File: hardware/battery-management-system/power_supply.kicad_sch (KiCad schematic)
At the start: 42 parts, among them J10 18V, J11 3V3, J9 5V, U1 ICL7660, U2 L6982C33DR, U3 L6982C33DR, U4 ICL7660

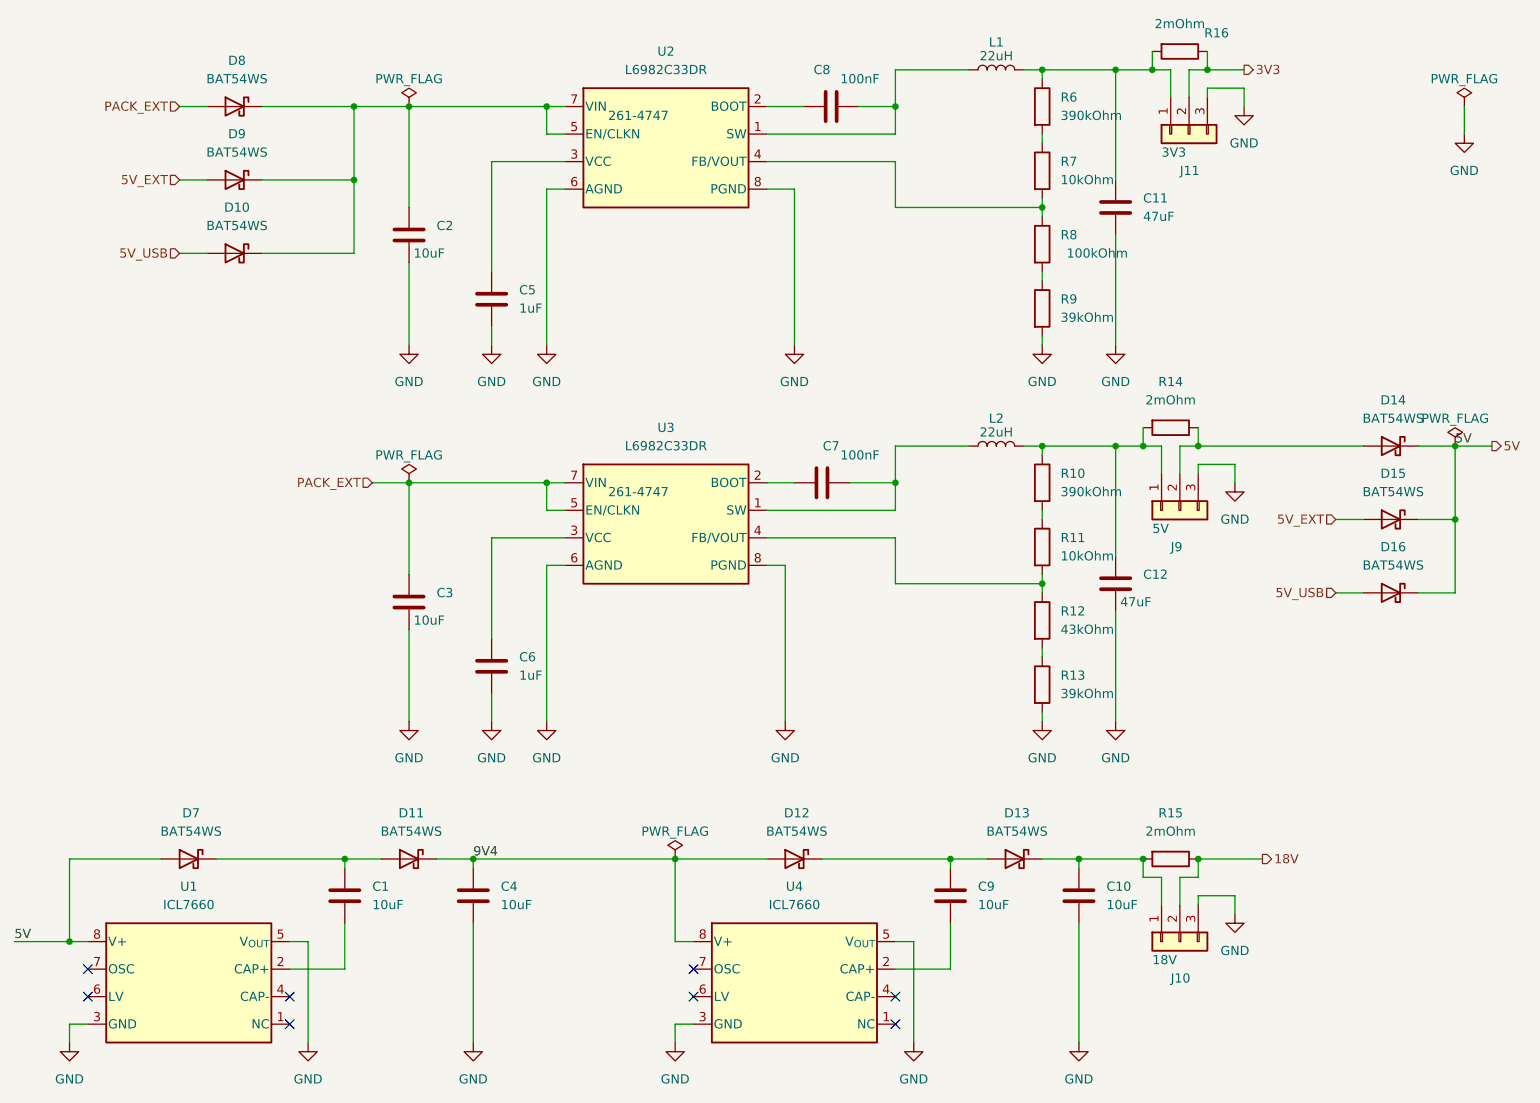
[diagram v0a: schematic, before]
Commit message: start simplifying BMS for R02
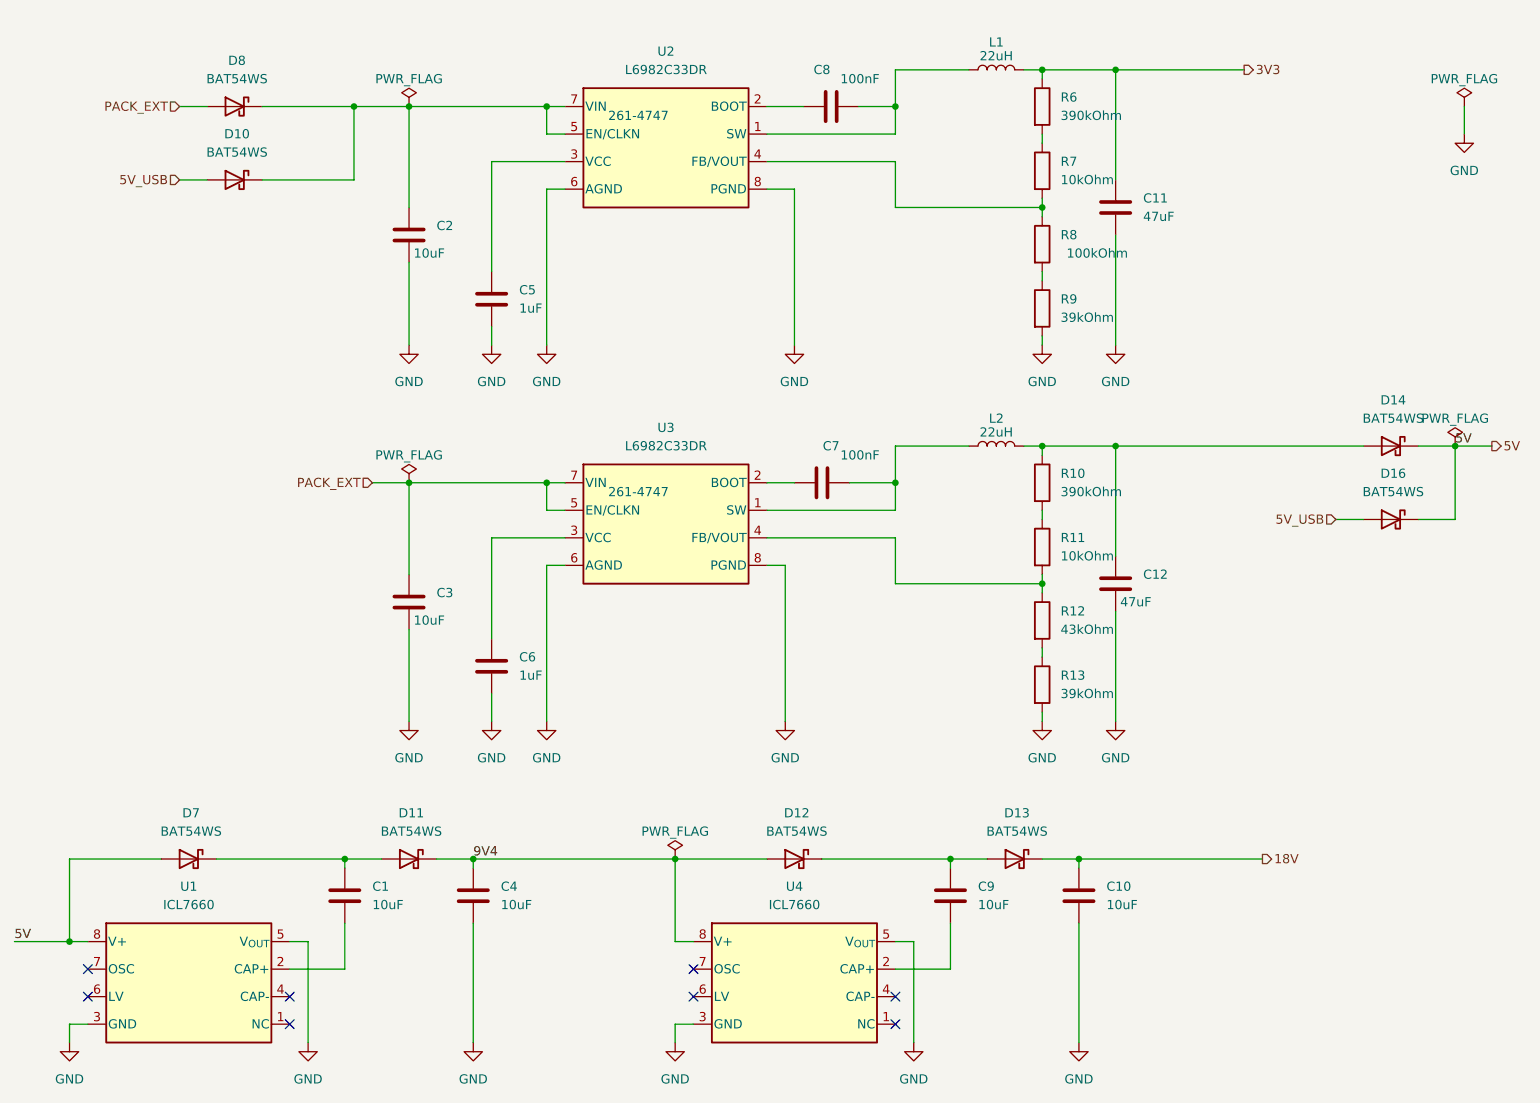
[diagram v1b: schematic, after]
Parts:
- removed D15, D9: BAT54WS, benediktibk:D_SOD-323, symbol benediktibk:BAT54WS
- removed J10: 18V, benediktibk:PinHeader_1x03_P2.54mm_Vertical, symbol benediktibk:Conn_01x03
- removed J11: 3V3, benediktibk:PinHeader_1x03_P2.54mm_Vertical, symbol benediktibk:Conn_01x03
- removed J9: 5V, benediktibk:PinHeader_1x03_P2.54mm_Vertical, symbol benediktibk:Conn_01x03
- removed R14, R15, R16: 2mOhm, benediktibk:R_2512_6332Metric_Pad1.40x3.35mm_HandSolder, symbol benediktibk:R_2mOhm_SMD_2512_5W_1%
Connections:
- net 18V: now also C10.1, D13.1 (K)
- net 3V3: now also C11.1, L1.1, R6.1
- net at C12.1, L2.1, R10.1: now also D14.2 (A)
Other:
- moved on the sheet: D10, D16

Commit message: fix design errors
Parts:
- L1, L2: symbol benediktibk:L_22uH_2A_10% -> benediktibk:L_22uH_1_9A_9MHz_10%
- U2, U3: value L6982C33DR -> L6982CDR; symbol benediktibk:L6982C33DR -> benediktibk:L6982CDR; RS order number 261-4747 -> 228-2997
- renumbered D11 to D10, D12 to D11, D13 to D12, D14 to D13, D16 to D14, D10 to D9, R9 to R10, R10 to R11, R11 to R12, R12 to R13, R13 to R14, R6 to R7, R7 to R8, R8 to R9

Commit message: fix design errors
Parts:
- renumbered D12 to D10, D13 to D11, D14 to D12, D7 to D5, D8 to D6, D9 to D7, D10 to D8, D11 to D9
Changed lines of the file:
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@@
   (symbol (lib_id "benediktibk:BAT54WS") (at 74.93 129.54 0) (mirror y) (unit 1)
     (in_bom yes) (on_board yes) (dnp no) (fields_autoplaced)
-    (property "Reference" "D10" (at 75.2475 123.19 0)
+    (property "Reference" "D8" (at 75.2475 123.19 0)
       (effects (font (size 1.27 1.27)))
     )
@@
       (project "battery-management-system"
         (path "/5272f0ff-3069-41a9-bca2-80beede8b4b2/b1377397-46a1-4623-af59-88e4e694ca35"
-          (reference "D10") (unit 1)
+          (reference "D8") (unit 1)
         )
       )
@@
   (symbol (lib_id "benediktibk:BAT54WS") (at 210.82 72.39 0) (mirror y) (unit 1)
     (in_bom yes) (on_board yes) (dnp no) (fields_autoplaced)
-    (property "Reference" "D13" (at 211.1375 66.04 0)
+    (property "Reference" "D11" (at 211.1375 66.04 0)
       (effects (font (size 1.27 1.27)))
     )
@@
       (project "battery-management-system"
         (path "/5272f0ff-3069-41a9-bca2-80beede8b4b2/b1377397-46a1-4623-af59-88e4e694ca35"
-          (reference "D13") (unit 1)
+          (reference "D11") (unit 1)
         )
       )
@@
   (symbol (lib_id "benediktibk:BAT54WS") (at 128.27 129.54 0) (mirror y) (unit 1)
     (in_bom yes) (on_board yes) (dnp no) (fields_autoplaced)
-    (property "Reference" "D11" (at 128.5875 123.19 0)
+    (property "Reference" "D9" (at 128.5875 123.19 0)
       (effects (font (size 1.27 1.27)))
     )
@@
       (project "battery-management-system"
         (path "/5272f0ff-3069-41a9-bca2-80beede8b4b2/b1377397-46a1-4623-af59-88e4e694ca35"
-          (reference "D11") (unit 1)
+          (reference "D9") (unit 1)
         )
       )
@@
   (symbol (lib_id "benediktibk:BAT54WS") (at 50.8 25.4 0) (mirror y) (unit 1)
     (in_bom yes) (on_board yes) (dnp no) (fields_autoplaced)
-    (property "Reference" "D8" (at 51.1175 19.05 0)
+    (property "Reference" "D6" (at 51.1175 19.05 0)
       (effects (font (size 1.27 1.27)))
     )
@@
       (project "battery-management-system"
         (path "/5272f0ff-3069-41a9-bca2-80beede8b4b2/b1377397-46a1-4623-af59-88e4e694ca35"
-          (reference "D8") (unit 1)
+          (reference "D6") (unit 1)
         )
       )
@@
   (symbol (lib_id "benediktibk:BAT54WS") (at 158.75 129.54 0) (mirror y) (unit 1)
     (in_bom yes) (on_board yes) (dnp no) (fields_autoplaced)
-    (property "Reference" "D12" (at 159.0675 123.19 0)
+    (property "Reference" "D10" (at 159.0675 123.19 0)
       (effects (font (size 1.27 1.27)))
     )
@@
       (project "battery-management-system"
         (path "/5272f0ff-3069-41a9-bca2-80beede8b4b2/b1377397-46a1-4623-af59-88e4e694ca35"
-          (reference "D12") (unit 1)
+          (reference "D10") (unit 1)
         )
       )
@@
   (symbol (lib_id "benediktibk:BAT54WS") (at 210.82 82.55 0) (mirror y) (unit 1)
     (in_bom yes) (on_board yes) (dnp no) (fields_autoplaced)
-    (property "Reference" "D14" (at 211.1375 76.2 0)
+    (property "Reference" "D12" (at 211.1375 76.2 0)
       (effects (font (size 1.27 1.27)))
     )
@@
       (project "battery-management-system"
         (path "/5272f0ff-3069-41a9-bca2-80beede8b4b2/b1377397-46a1-4623-af59-88e4e694ca35"
-          (reference "D14") (unit 1)
+          (reference "D12") (unit 1)
         )
       )
@@
   (symbol (lib_id "benediktibk:BAT54WS") (at 50.8 35.56 0) (mirror y) (unit 1)
     (in_bom yes) (on_board yes) (dnp no) (fields_autoplaced)
-    (property "Reference" "D9" (at 51.1175 29.21 0)
+    (property "Reference" "D7" (at 51.1175 29.21 0)
       (effects (font (size 1.27 1.27)))
     )
@@
       (project "battery-management-system"
         (path "/5272f0ff-3069-41a9-bca2-80beede8b4b2/b1377397-46a1-4623-af59-88e4e694ca35"
-          (reference "D9") (unit 1)
+          (reference "D7") (unit 1)
         )
       )
@@
   (symbol (lib_id "benediktibk:BAT54WS") (at 44.45 129.54 0) (mirror y) (unit 1)
     (in_bom yes) (on_board yes) (dnp no) (fields_autoplaced)
-    (property "Reference" "D7" (at 44.7675 123.19 0)
+    (property "Reference" "D5" (at 44.7675 123.19 0)
       (effects (font (size 1.27 1.27)))
     )
@@
       (project "battery-management-system"
         (path "/5272f0ff-3069-41a9-bca2-80beede8b4b2/b1377397-46a1-4623-af59-88e4e694ca35"
-          (reference "D7") (unit 1)
-        )
-      )
+          (reference "D5") (unit 1)
+        )
+      )

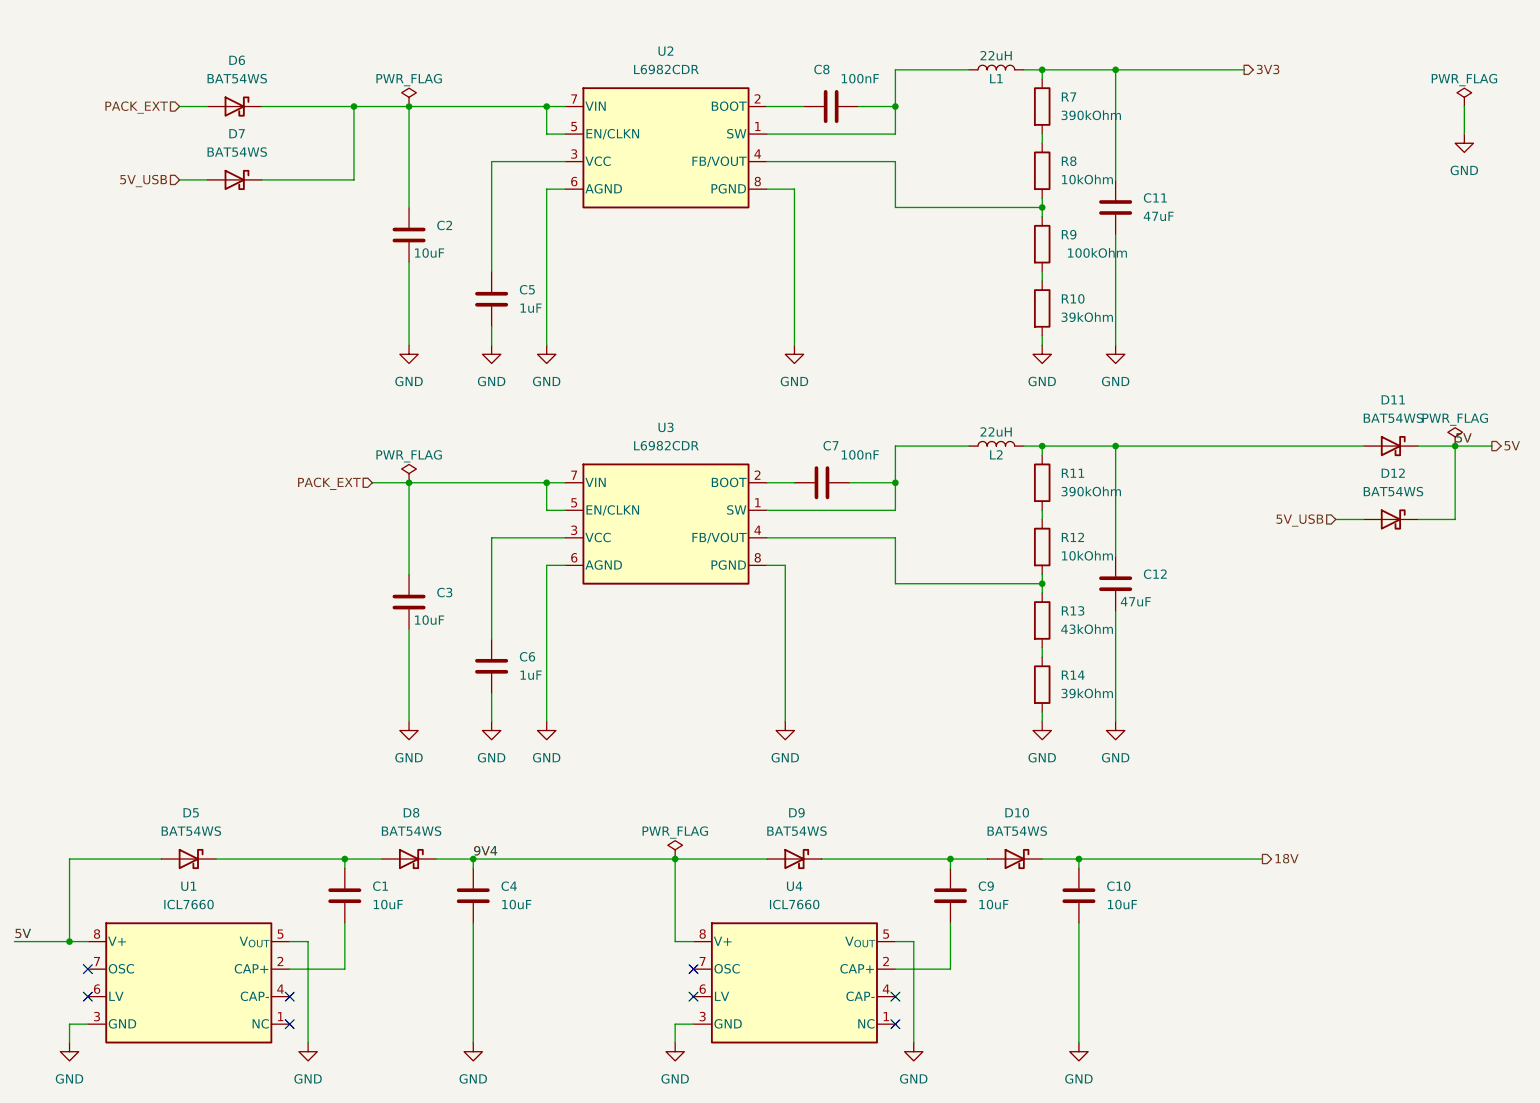
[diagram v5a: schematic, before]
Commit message: add snubber circuit
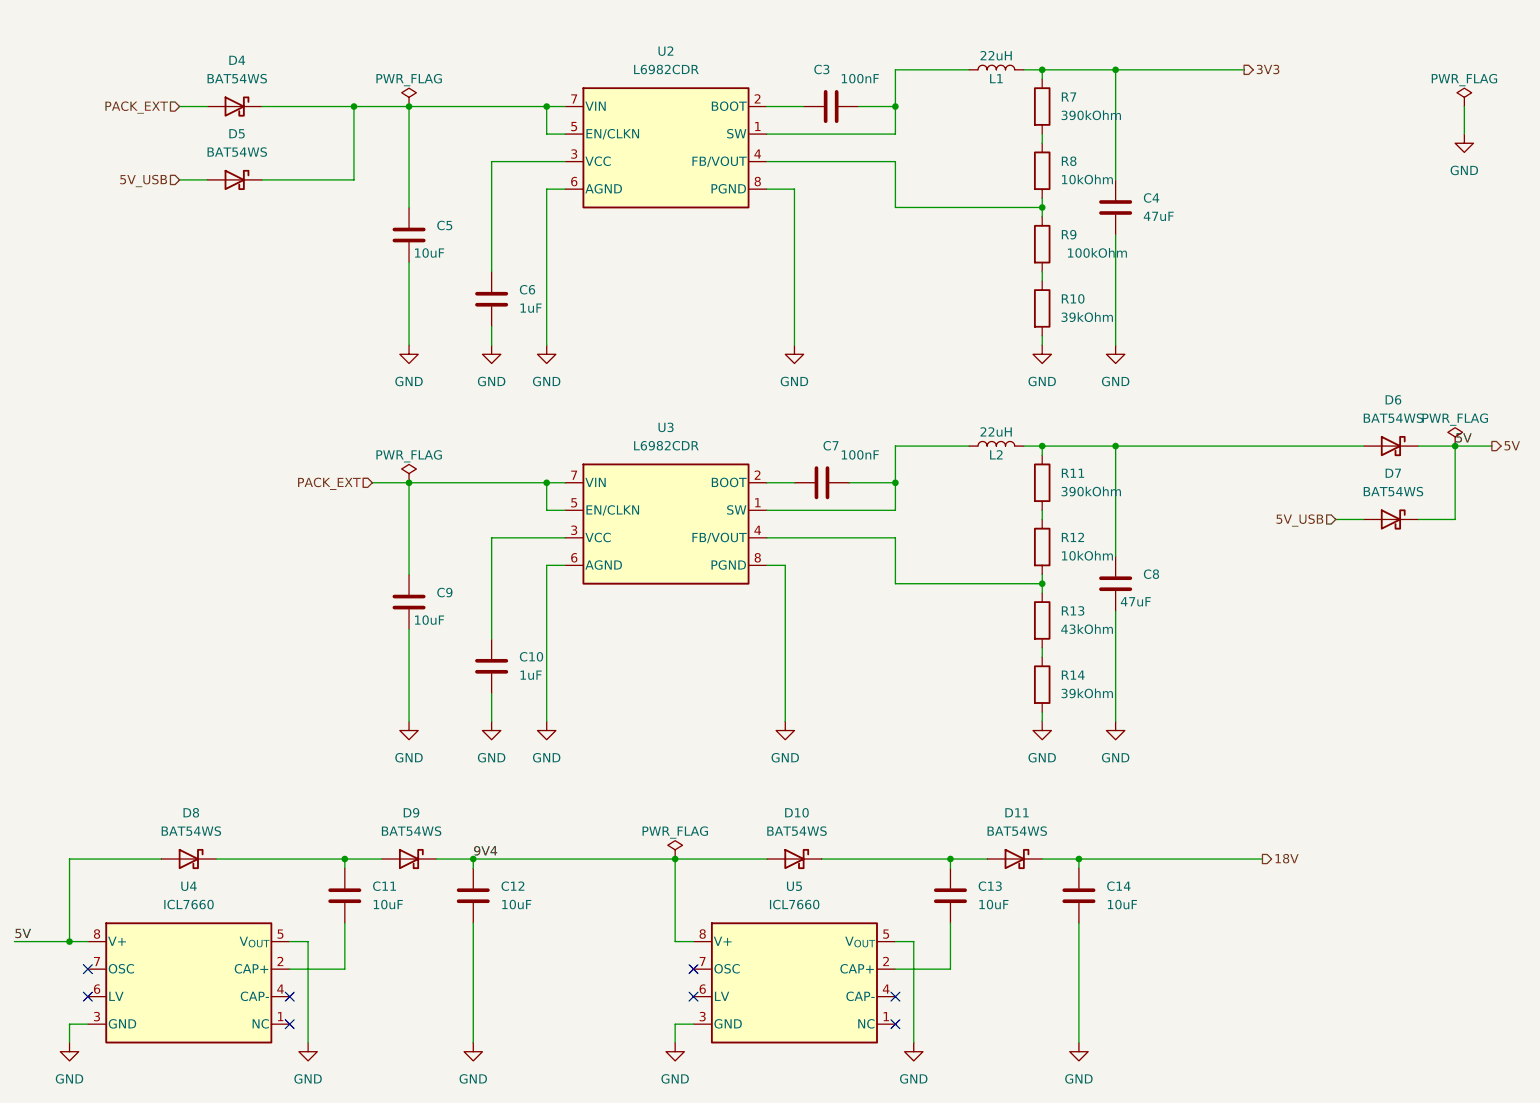
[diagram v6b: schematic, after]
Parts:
- renumbered C6 to C10, C1 to C11, C4 to C12, C9 to C13, C10 to C14, C8 to C3, C11 to C4, C2 to C5, C5 to C6, C12 to C8, C3 to C9, D9 to D10, D10 to D11, D6 to D4, D7 to D5, D11 to D6, D12 to D7, D5 to D8, D8 to D9, U1 to U4, U4 to U5

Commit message: update symbols from library
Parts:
- C10, C6: Mouser Part Number (none) -> 963-UMK107BJ105KA-T
- C11, C12, C13, C14, C5, C9: Mouser Part Number (none) -> 187-CL31A106MBHNNNE
- C3, C7: Mouser Part Number (none) -> 581-KGM15BR71H104KM
- C4, C8: Mouser Part Number (none) -> 810-C3216X5R1E476M
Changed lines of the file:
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@@
+			)
+		)
+		(property "Mouser Part Number" "187-CL31A106MBHNNNE"
+			(at 101.346 133.35 0)
+			(effects
+				(font
+					(size 1.27 1.27)
+				)
+				(hide yes)
 			)
 		)
@@
 			)
 		)
+		(property "Mouser Part Number" "581-KGM15BR71H104KM"
+			(at 133.35 94.996 0)
+			(effects
+				(font
+					(size 1.27 1.27)
+				)
+				(hide yes)
+			)
+		)
 		(pin "1"
 		)
@@
 			)
 		)
+		(property "Mouser Part Number" "187-CL31A106MBHNNNE"
+			(at 83.566 133.35 0)
+			(effects
+				(font
+					(size 1.27 1.27)
+				)
+				(hide yes)
+			)
+		)
 		(pin "2"
 		)
@@
 			)
 		)
+		(property "Mouser Part Number" "810-C3216X5R1E476M"
+			(at 190.246 38.1 0)
+			(effects
+				(font
+					(size 1.27 1.27)
+				)
+				(hide yes)
+			)
+		)
 		(pin "1"
 		)
@@
 			)
 		)
+		(property "Mouser Part Number" "187-CL31A106MBHNNNE"
+			(at 92.456 92.71 0)
+			(effects
+				(font
+					(size 1.27 1.27)
+				)
+				(hide yes)
+			)
+		)
 		(pin "1"
 		)
@@
 			)
 		)
+		(property "Mouser Part Number" "963-UMK107BJ105KA-T"
+			(at 103.886 101.6 0)
+			(effects
+				(font
+					(size 1.27 1.27)
+				)
+				(hide yes)
+			)
+		)
 		(pin "1"
 		)
@@
 			)
 		)
+		(property "Mouser Part Number" "187-CL31A106MBHNNNE"
+			(at 92.456 41.91 0)
+			(effects
+				(font
+					(size 1.27 1.27)
+				)
+				(hide yes)
+			)
+		)
 		(pin "1"
 		)
@@
 			)
 		)
+		(property "Mouser Part Number" "187-CL31A106MBHNNNE"
+			(at 167.386 133.35 0)
+			(effects
+				(font
+					(size 1.27 1.27)
+				)
+				(hide yes)
+			)
+		)
 		(pin "2"
 		)
@@
 			)
 		)
+		(property "Mouser Part Number" "963-UMK107BJ105KA-T"
+			(at 103.886 50.8 0)
+			(effects
+				(font
+					(size 1.27 1.27)
+				)
+				(hide yes)
+			)
+		)
 		(pin "1"
 		)
@@
 			)
 		)
+		(property "Mouser Part Number" "810-C3216X5R1E476M"
+			(at 190.246 90.17 0)
+			(effects
+				(font
+					(size 1.27 1.27)
+				)
+				(hide yes)
+			)
+		)
 		(pin "1"
 		)
@@
 			)
 		)
+		(property "Mouser Part Number" "581-KGM15BR71H104KM"
+			(at 134.62 42.926 0)
+			(effects
+				(font
+					(size 1.27 1.27)
+				)
+				(hide yes)
+			)
+		)
 		(pin "1"
 		)
@@
 			(at 185.166 133.35 0)
 			(effects
+				(font
+					(size 1.27 1.27)
+				)
+				(hide yes)
+			)
+		)
+		(property "Mouser Part Number" "187-CL31A106MBHNNNE"
+			(at 185.166 133.35 0)
+			(effects
